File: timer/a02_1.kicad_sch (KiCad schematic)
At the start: 7 parts, among them U2103 74HC04, U2104 74HC02, U2105 74HC04, U2108 74HC04, U2109 74HC02, U2110 74HC04, U2148 74LVC06

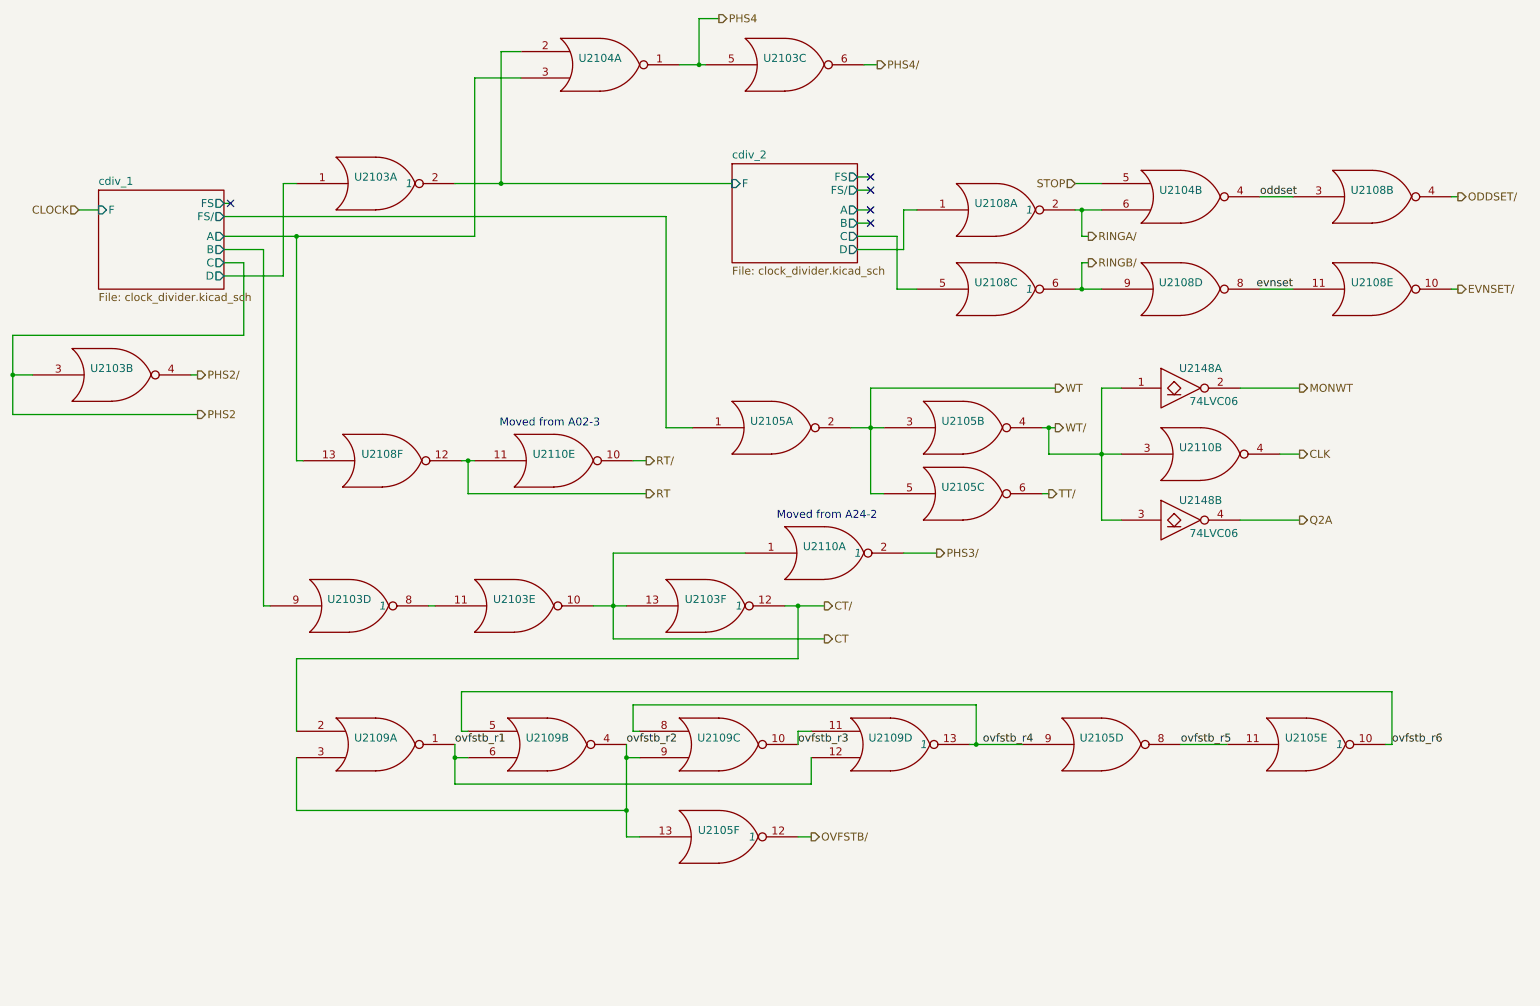
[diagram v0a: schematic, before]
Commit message: Added Init values
Added individual Init Values for Components. TImer Module Updated with init values
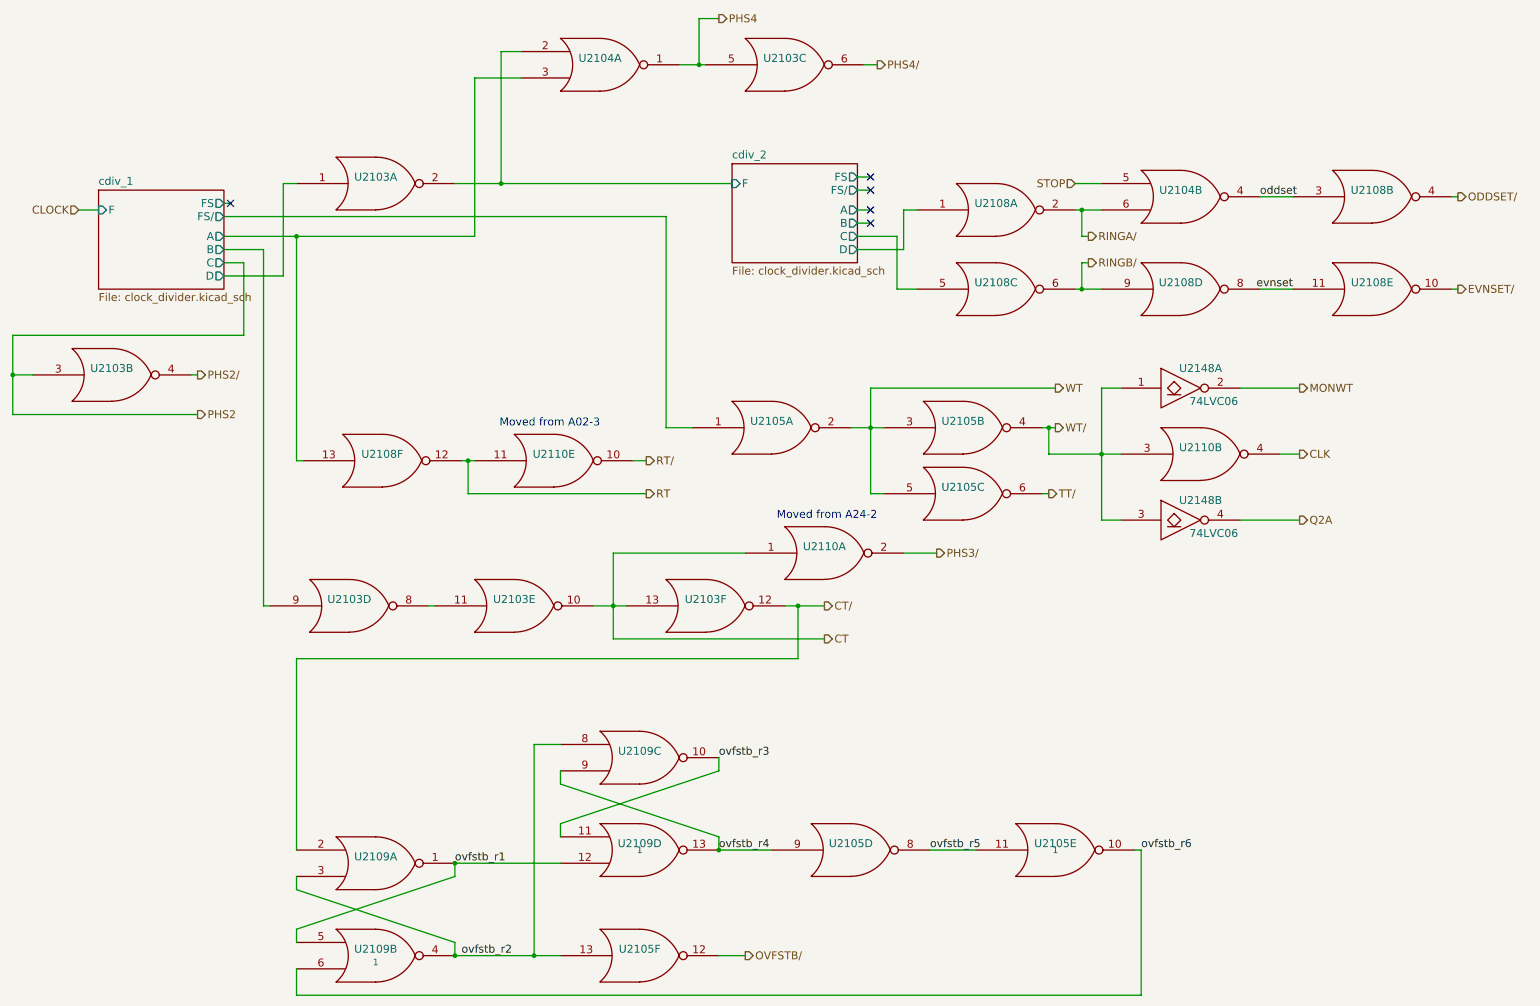
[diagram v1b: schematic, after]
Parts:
- U2103, U2108, U2110: Init_A (none) -> 0; Init_B (none) -> 0; Init_C (none) -> 0; Init_D (none) -> 0; Init_E (none) -> 0; Init_F (none) -> 0; Initial 1 -> (none)
- U2103, U2108, U2110: Init_A (none) -> 0; Init_B (none) -> 0; Init_C (none) -> 0; Init_D (none) -> 0; Init_E (none) -> 0; Init_F (none) -> 0
- U2104: Init_A (none) -> 0; Init_B (none) -> 0; Init_C (none) -> 0; Init_D (none) -> 0
- U2105: Init_A (none) -> 0; Init_B (none) -> 0; Init_C (none) -> 0; Init_D (none) -> 0; Init_E (none) -> 1; Init_F (none) -> 0
- U2105: Init_A (none) -> 0; Init_B (none) -> 0; Init_C (none) -> 0; Init_D (none) -> 0; Init_E (none) -> 1; Init_F (none) -> 0; Initial 1 -> (none)
- U2109: Init_A (none) -> 0; Init_B (none) -> 1; Init_C (none) -> 0; Init_D (none) -> 1
- U2109: Init_A (none) -> 0; Init_B (none) -> 1; Init_C (none) -> 0; Init_D (none) -> 1; Initial 1 -> (none)
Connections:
- net ovfstb_r1: now also U2109.5; no longer U2109.6
- net ovfstb_r2: now also U2109.8; no longer U2109.9
- net ovfstb_r4: now also U2109.9; no longer U2109.8
- net ovfstb_r6: now also U2109.6; no longer U2109.5
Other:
- moved on the sheet: U2105D, U2105E, U2105F, U2109A, U2109B, U2109C, U2109D
